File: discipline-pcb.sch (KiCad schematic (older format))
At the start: 169 parts, among them J1 AVR-ISP-6, SW1 KEYSW, SW10 KEYSW, SW11 KEYSW, SW12 KEYSW, SW13 KEYSW, SW14 KEYSW, SW15 KEYSW, SW16 KEYSW, SW17 KEYSW, SW18 KEYSW, SW19 KEYSW, SW2 KEYSW, SW20 KEYSW, SW21 KEYSW, SW22 KEYSW, SW23 KEYSW, SW24 KEYSW, SW25 KEYSW, SW26 KEYSW, SW27 KEYSW, SW28 KEYSW, SW29 KEYSW, SW3 KEYSW, SW30 KEYSW, SW31 KEYSW, SW32 KEYSW, SW33 KEYSW, SW34 KEYSW, SW35 KEYSW, SW36 KEYSW, SW37 KEYSW, SW38 KEYSW, SW39 KEYSW, SW4 KEYSW, SW40 KEYSW, SW41 KEYSW, SW42 KEYSW, SW43 KEYSW, SW44 KEYSW, SW45 KEYSW, SW46 KEYSW, SW47 KEYSW, SW48 KEYSW, SW49 KEYSW, SW5 KEYSW, SW50 KEYSW, SW51 KEYSW, SW52 KEYSW, SW53 KEYSW, SW54 KEYSW, SW55 KEYSW, SW56 KEYSW, SW57 KEYSW, SW58 KEYSW, SW59 KEYSW, SW6 KEYSW, SW60 KEYSW, SW61 KEYSW, SW62 KEYSW, SW63 KEYSW, SW64 KEYSW, SW65 KEYSW, SW66 KEYSW, SW67 KEYSW, SW68 KEYSW, SW69 KEYSW, SW7 KEYSW, SW70 KEYSW, SW71 KEYSW, SW72 KEYSW, SW73 KEYSW, SW74 KEYSW, SW75 KEYSW, SW76 KEYSW, SW77 KEYSW, SW78 KEYSW, SW8 KEYSW, SW9 KEYSW, U1 ATmega32A-PU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

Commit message: Replace keyswitch footprint with MX_Alps_Hybrid
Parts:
- SW1, SW10, SW11, SW12, SW13, SW15, SW17, SW18, SW19, SW2, SW20, SW21, SW22, SW23, SW24, SW25, SW26, SW27, SW28, SW3, SW30, SW32, SW33, SW34, SW35, SW36, SW37, SW38, SW39, SW4, SW40, SW41, SW42, SW44, SW46, SW47, SW48, SW49, SW5, SW50, SW51, SW52, SW53, SW54, SW55, SW57, SW58, SW6, SW62, SW65, SW66, SW67, SW68, SW7, SW72, SW75, SW77, SW8, SW9: footprint cftkb:SW_Cherry_MX1A_1.00u_PCB-NOSCREEN -> MX_Alps_Hybrid:MX-1U
- SW14: footprint cftkb:SW_Cherry_MX1A_2.00u_PCBNOSCREEN -> MX_Alps_Hybrid:MX-2U
- SW16, SW29, SW70, SW71, SW73, SW74: footprint cftkb:SW_Cherry_MX1A_1.50u_PCBNOSCREEN -> MX_Alps_Hybrid:MX-1.5U
- SW31, SW56: footprint cftkb:SW_Cherry_MX1A_1.75u_PCBNOSCREEN -> MX_Alps_Hybrid:MX-1.75U
- SW43, SW45: footprint cftkb:SW_Cherry_MX1A_2.25u_PCBNOSCREEN -> MX_Alps_Hybrid:MX-2.25U
- SW59, SW60, SW61, SW63, SW64, SW69, SW78: footprint cftkb:SW_Cherry_MX1A_1.25u_PCBNOSCREEN -> MX_Alps_Hybrid:MX-1.25U
- SW76: footprint cftkb:SW_Cherry_MX1A_ISOEnter_PCB_ReversedStabilizer -> cftkb:MX_Alps_Hybrid_ISOEnter_PCB_ReversedStabilizer

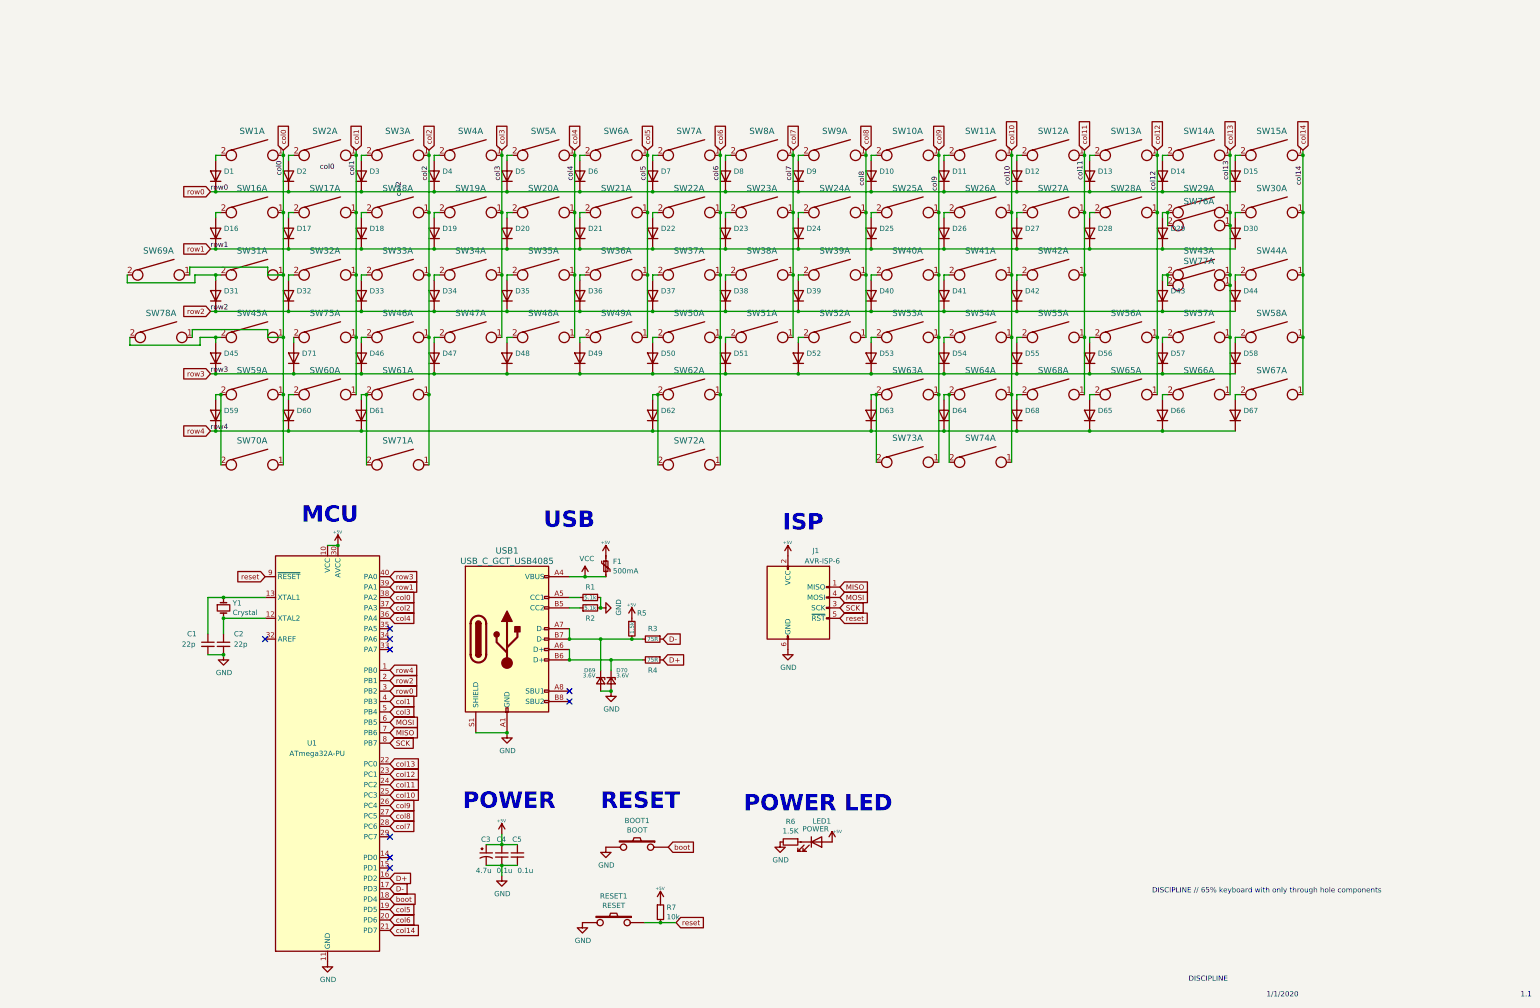
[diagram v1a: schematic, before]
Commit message: Remove ISO layout, add led matrix to schematic
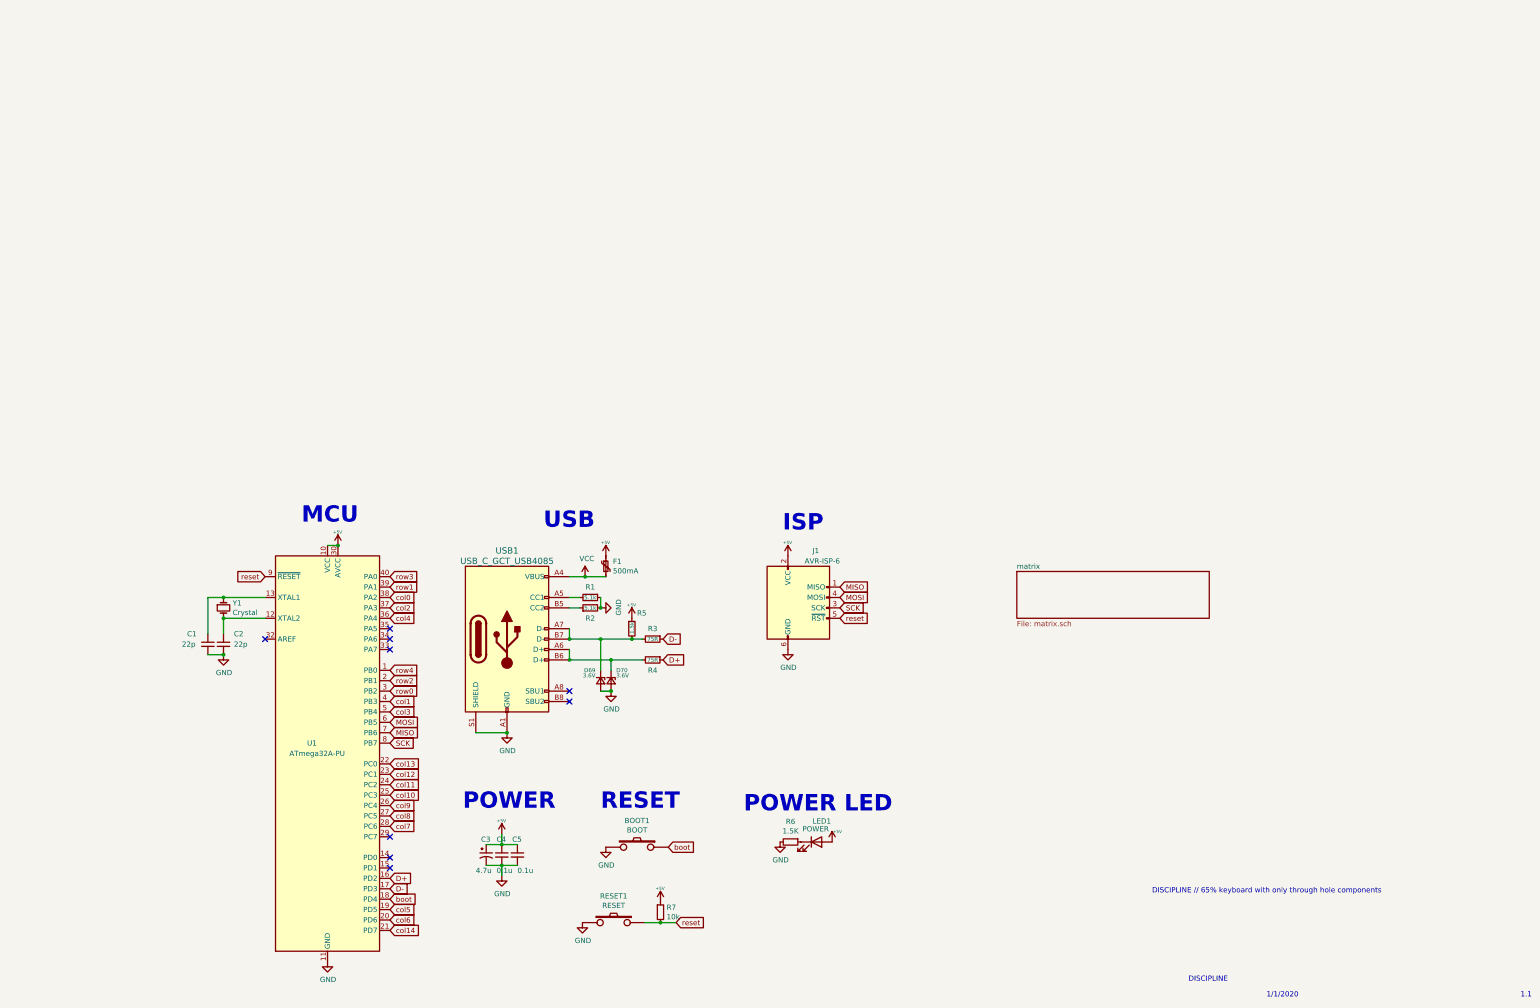
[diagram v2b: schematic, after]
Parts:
- removed D1, D10, D11, D12, D13, D14, D15, D16, D17, D18, D19, D2, D20, D21, D22, D23, D24, D25, D26, D27, D28, D29, D3, D30, D31, D32, D33, D34, D35, D36, D37, D38, D39, D4, D40, D41, D42, D43, D44, D45, D46, D47, D48, D49, D5, D50, D51, D52, D53, D54, D55, D56, D57, D58, D59, D6, D60, D61, D62, D63, D64, D65, D66, D67, D68, D7, D71, D8, D9: (no value), cftkb:D_DO-35_SOD27_P5.08mm_Horizontal, symbol Device:D
- removed SW1, SW10, SW11, SW12, SW13, SW15, SW17, SW18, SW19, SW2, SW20, SW21, SW22, SW23, SW24, SW25, SW26, SW27, SW28, SW3, SW30, SW32, SW33, SW34, SW35, SW36, SW37, SW38, SW39, SW4, SW40, SW41, SW42, SW44, SW46, SW47, SW48, SW49, SW5, SW50, SW51, SW52, SW53, SW54, SW55, SW57, SW58, SW6, SW62, SW65, SW66, SW67, SW68, SW7, SW72, SW75, SW77, SW8, SW9: KEYSW, MX_Alps_Hybrid:MX-1U, symbol keyboard_parts:KEYSW
- removed SW14: KEYSW, MX_Alps_Hybrid:MX-2U, symbol keyboard_parts:KEYSW
- removed SW16, SW29, SW70, SW71, SW73, SW74: KEYSW, MX_Alps_Hybrid:MX-1.5U, symbol keyboard_parts:KEYSW
- removed SW31, SW56: KEYSW, MX_Alps_Hybrid:MX-1.75U, symbol keyboard_parts:KEYSW
- removed SW43, SW45: KEYSW, MX_Alps_Hybrid:MX-2.25U, symbol keyboard_parts:KEYSW
- removed SW59, SW60, SW61, SW63, SW64, SW69, SW78: KEYSW, MX_Alps_Hybrid:MX-1.25U, symbol keyboard_parts:KEYSW
- removed SW76: KEYSW, cftkb:MX_Alps_Hybrid_ISOEnter_PCB_ReversedStabilizer, symbol keyboard_parts:KEYSW

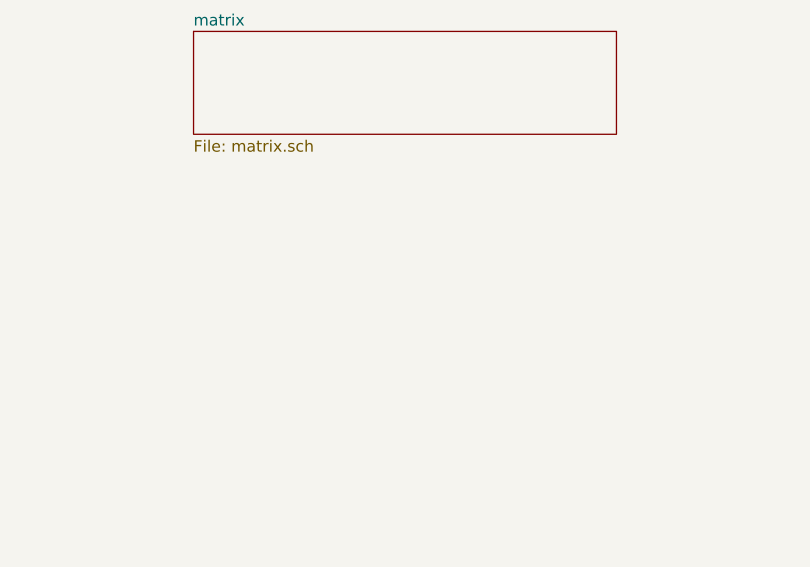
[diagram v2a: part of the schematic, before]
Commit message: Misc cleanup, delete tracks to prepare for bigger changes
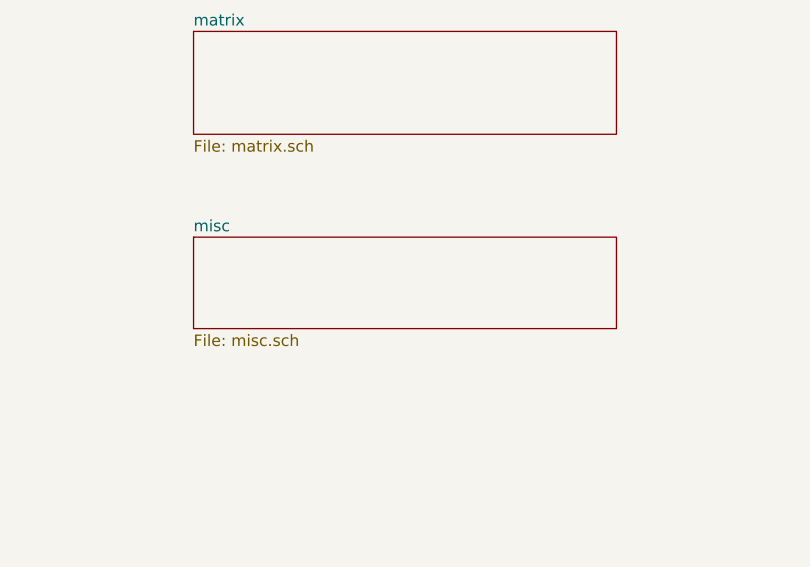
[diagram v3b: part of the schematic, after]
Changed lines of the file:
@@
 $Descr A3 16535 11693
 encoding utf-8
-Sheet 1 2
+Sheet 1 3
 Title ""
 Date ""
@@
 F1 "matrix.sch" 50
 $EndSheet
+$Sheet
+S 10600 7850 1850 400
+U 62088CFF
+F0 "misc" 50
+F1 "misc.sch" 50
+$EndSheet
 $EndSCHEMATC

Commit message: Move diodes to key area
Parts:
- D69, D70: footprint cftkb:D_DO-35_SOD27_P5.08mm_Horizontal -> keyboard_parts:D_SOD123_axial
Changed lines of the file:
@@
 F 0 "D69" V 6500 7950 39  0000 R CNN
 F 1 "3.6V" V 6550 7950 39  0000 R CNN
-F 2 "cftkb:D_DO-35_SOD27_P5.08mm_Horizontal" V 6600 8000 50  0001 C CNN
+F 2 "keyboard_parts:D_SOD123_axial" V 6600 8000 50  0001 C CNN
 F 3 "~" V 6600 8000 50  0001 C CNN
 	1    6600 8000
@@
 F 0 "D70" V 6600 8050 39  0000 L CNN
 F 1 "3.6V" V 6650 8050 39  0000 L CNN
-F 2 "cftkb:D_DO-35_SOD27_P5.08mm_Horizontal" V 6700 8000 50  0001 C CNN
+F 2 "keyboard_parts:D_SOD123_axial" V 6700 8000 50  0001 C CNN
 F 3 "~" V 6700 8000 50  0001 C CNN
 	1    6700 8000
